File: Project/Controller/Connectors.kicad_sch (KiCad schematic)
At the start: 24 parts, among them J10 Servo, J11 Servo, J12 Servo, J13 Thruster, J14 I2C, J15 I2C, J16 UART1, J17 UART2, J18 SPI1, J19 SPI2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

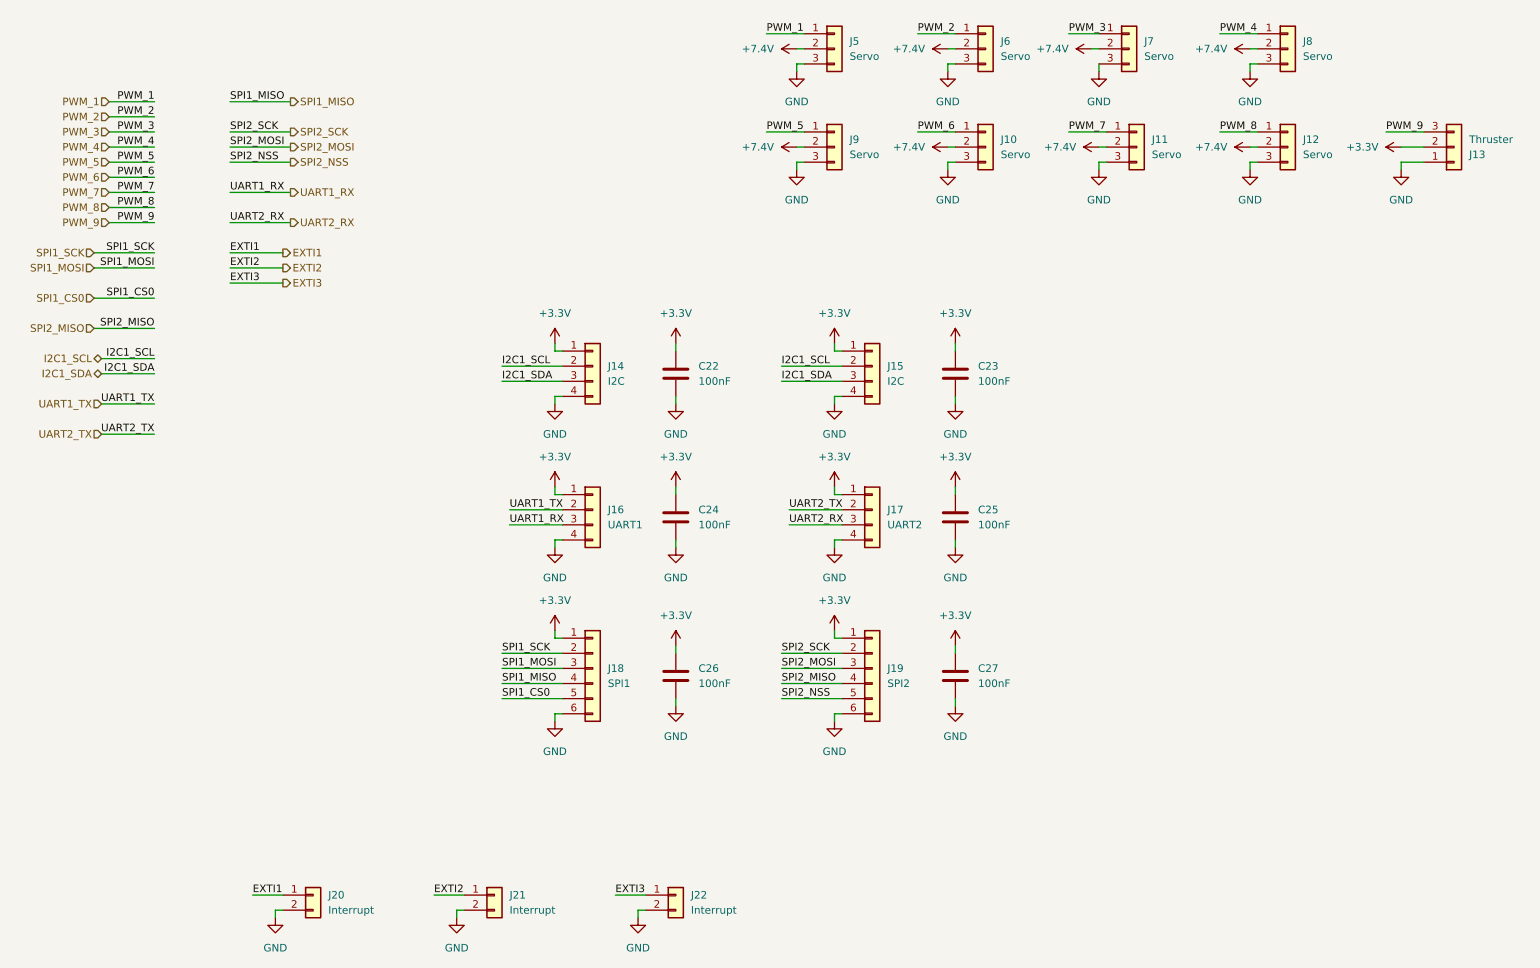
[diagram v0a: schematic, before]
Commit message: Remove battery power from servo PWM connector
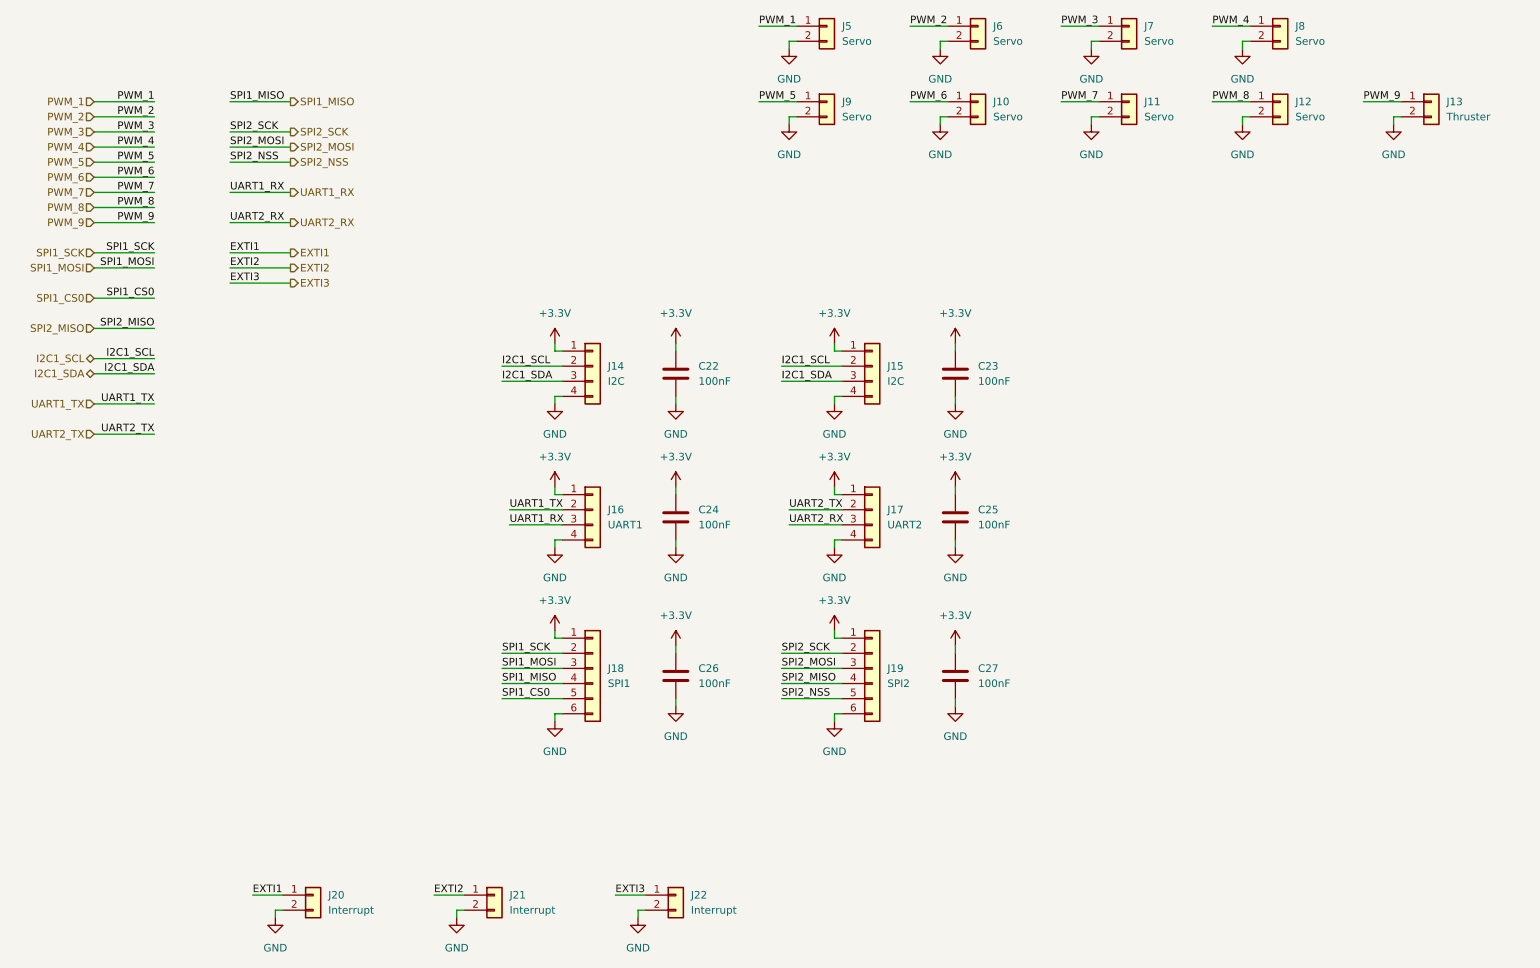
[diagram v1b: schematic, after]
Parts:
- removed J10, J11, J12, J5, J6, J7, J8, J9: Servo, Connector_JST:JST_VH_B3P-VH-B_1x03_P3.96mm_Vertical, symbol Connector_Generic:Conn_01x03
- removed J13: Thruster, Connector_JST:JST_VH_B3P-VH-B_1x03_P3.96mm_Vertical, symbol Connector_Generic:Conn_01x03
- added J10, J11, J12, J5, J6, J7, J8, J9: Servo, Connector_JST:JST_VH_B2P-VH_1x02_P3.96mm_Vertical, symbol Connector_Generic:Conn_01x02
- added J13: Thruster, Connector_JST:JST_VH_B2P-VH_1x02_P3.96mm_Vertical, symbol Connector_Generic:Conn_01x02
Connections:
- net GND: now also J10.2 (Pin_2), J11.2 (Pin_2), J12.2 (Pin_2), J13.2 (Pin_2), J5.2 (Pin_2), J6.2 (Pin_2), J7.2 (Pin_2), J8.2 (Pin_2), J9.2 (Pin_2)
- net PWM_1: now also J5.1 (Pin_1)
- net PWM_2: now also J6.1 (Pin_1)
- net PWM_3: now also J7.1 (Pin_1)
- net PWM_4: now also J8.1 (Pin_1)
- net PWM_5: now also J9.1 (Pin_1)
- net PWM_6: now also J10.1 (Pin_1)
- net PWM_7: now also J11.1 (Pin_1)
- net PWM_8: now also J12.1 (Pin_1)
- net PWM_9: now also J13.1 (Pin_1)

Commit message: Change peripheral connectors to JST GH
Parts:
- J14, J15, J16, J17: footprint Connector_Molex:Molex_PicoBlade_53048-0410_1x04_P1.25mm_Horizontal -> Connector_JST:JST_GH_SM04B-GHS-TB_1x04-1MP_P1.25mm_Horizontal; Listing https://www.digikey.com/en/products/detail/molex/0530480410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 -> https://www.digikey.com/en/products/detail/jst-sales-americ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
- J18, J19: footprint Connector_Molex:Molex_PicoBlade_53048-0610_1x06_P1.25mm_Horizontal -> Connector_JST:JST_GH_SM06B-GHS-TB_1x06-1MP_P1.25mm_Horizontal; Listing https://www.digikey.com/en/products/detail/molex/0530480610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 -> https://www.digikey.com/en/products/detail/jst-sales-americ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
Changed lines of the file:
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@@
 			)
 		)
-		(property "Footprint" "Connector_Molex:Molex_PicoBlade_53048-0610_1x06_P1.25mm_Horizontal"
+		(property "Footprint" "Connector_JST:JST_GH_SM06B-GHS-TB_1x06-1MP_P1.25mm_Horizontal"
 			(at 124.46 133.35 0)
 			(effects
@@
 			)
 		)
-		(property "Datasheet" "https://www.molex.com/content/dam/molex/molex-dot-com/products/automated/en-us/salesdrawingpdf/530/53048/530480610_sd.pdf?inline"
+		(property "Datasheet" "https://www.jst-mfg.com/product/pdf/eng/eGH.pdf"
 			(at 124.46 133.35 0)
 			(effects
@@
 			)
 		)
-		(property "Listing" "https://www.digikey.com/en/products/detail/molex/0530480610/242868"
+		(property "Listing" "https://www.digikey.com/en/products/detail/jst-sales-america-inc/SM06B-GHS-TB/807790"
 			(at 124.46 133.35 0)
 			(effects
@@
 			)
 		)
-		(property "Footprint" "Connector_Molex:Molex_PicoBlade_53048-0410_1x04_P1.25mm_Horizontal"
+		(property "Footprint" "Connector_JST:JST_GH_SM04B-GHS-TB_1x04-1MP_P1.25mm_Horizontal"
 			(at 124.46 106.68 0)
 			(effects
@@
 			)
 		)
-		(property "Datasheet" "https://www.molex.com/content/dam/molex/molex-dot-com/products/automated/en-us/salesdrawingpdf/530/53048/530480410_sd.pdf?inline"
+		(property "Datasheet" "https://www.jst-mfg.com/product/pdf/eng/eGH.pdf"
 			(at 124.46 106.68 0)
 			(effects
@@
 			)
 		)
-		(property "Listing" "https://www.digikey.com/en/products/detail/molex/0530480410/242866"
+		(property "Listing" "https://www.digikey.com/en/products/detail/jst-sales-america-inc/SM04B-GHS-TB/807788"
 			(at 124.46 106.68 0)
 			(effects
@@
 			)
 		)
-		(property "Footprint" "Connector_Molex:Molex_PicoBlade_53048-0410_1x04_P1.25mm_Horizontal"
+		(property "Footprint" "Connector_JST:JST_GH_SM04B-GHS-TB_1x04-1MP_P1.25mm_Horizontal"
 			(at 171.45 82.55 0)
 			(effects
@@
 			)
 		)
-		(property "Datasheet" "https://www.molex.com/content/dam/molex/molex-dot-com/products/automated/en-us/salesdrawingpdf/530/53048/530480410_sd.pdf?inline"
+		(property "Datasheet" "https://www.jst-mfg.com/product/pdf/eng/eGH.pdf"
 			(at 171.45 82.55 0)
 			(effects
@@
 			)
 		)
-		(property "Listing" "https://www.digikey.com/en/products/detail/molex/0530480410/242866"
+		(property "Listing" "https://www.digikey.com/en/products/detail/jst-sales-america-inc/SM04B-GHS-TB/807788"
 			(at 171.45 82.55 0)
 			(effects
@@
 			)
 		)
-		(property "Footprint" "Connector_Molex:Molex_PicoBlade_53048-0410_1x04_P1.25mm_Horizontal"
+		(property "Footprint" "Connector_JST:JST_GH_SM04B-GHS-TB_1x04-1MP_P1.25mm_Horizontal"
 			(at 124.46 82.55 0)
 			(effects
@@
 			)
 		)
-		(property "Datasheet" "https://www.molex.com/content/dam/molex/molex-dot-com/products/automated/en-us/salesdrawingpdf/530/53048/530480410_sd.pdf?inline"
+		(property "Datasheet" "https://www.jst-mfg.com/product/pdf/eng/eGH.pdf"
 			(at 124.46 82.55 0)
 			(effects
@@
 			)
 		)
-		(property "Listing" "https://www.digikey.com/en/products/detail/molex/0530480410/242866"
+		(property "Listing" "https://www.digikey.com/en/products/detail/jst-sales-america-inc/SM04B-GHS-TB/807788"
 			(at 124.46 82.55 0)
 			(effects
@@
 			)
 		)
-		(property "Footprint" "Connector_Molex:Molex_PicoBlade_53048-0610_1x06_P1.25mm_Horizontal"
+		(property "Footprint" "Connector_JST:JST_GH_SM06B-GHS-TB_1x06-1MP_P1.25mm_Horizontal"
 			(at 171.45 133.35 0)
 			(effects
@@
 			)
 		)
-		(property "Datasheet" "https://www.molex.com/content/dam/molex/molex-dot-com/products/automated/en-us/salesdrawingpdf/530/53048/530480610_sd.pdf?inline"
+		(property "Datasheet" "https://www.jst-mfg.com/product/pdf/eng/eGH.pdf"
 			(at 171.45 133.35 0)
 			(effects
@@
 			)
 		)
-		(property "Listing" "https://www.digikey.com/en/products/detail/molex/0530480610/242868"
+		(property "Listing" "https://www.digikey.com/en/products/detail/jst-sales-america-inc/SM06B-GHS-TB/807790"
 			(at 171.45 133.35 0)
 			(effects
@@
 			)
 		)
-		(property "Footprint" "Connector_Molex:Molex_PicoBlade_53048-0410_1x04_P1.25mm_Horizontal"
+		(property "Footprint" "Connector_JST:JST_GH_SM04B-GHS-TB_1x04-1MP_P1.25mm_Horizontal"
 			(at 171.45 106.68 0)
 			(effects
@@
 			)
 		)
-		(property "Datasheet" "https://www.molex.com/content/dam/molex/molex-dot-com/products/automated/en-us/salesdrawingpdf/530/53048/530480410_sd.pdf?inline"
+		(property "Datasheet" "https://www.jst-mfg.com/product/pdf/eng/eGH.pdf"
 			(at 171.45 106.68 0)
 			(effects
@@
 			)
 		)
-		(property "Listing" "https://www.digikey.com/en/products/detail/molex/0530480410/242866"
+		(property "Listing" "https://www.digikey.com/en/products/detail/jst-sales-america-inc/SM04B-GHS-TB/807788"
 			(at 171.45 106.68 0)
 			(effects

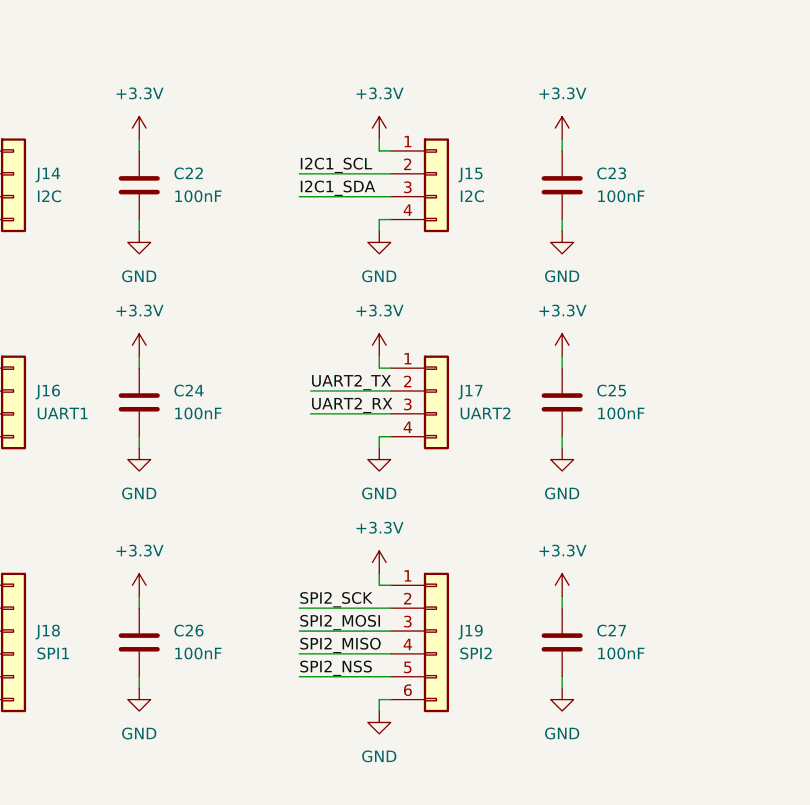
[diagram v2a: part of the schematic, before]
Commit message: Add LDO to power input for controller board
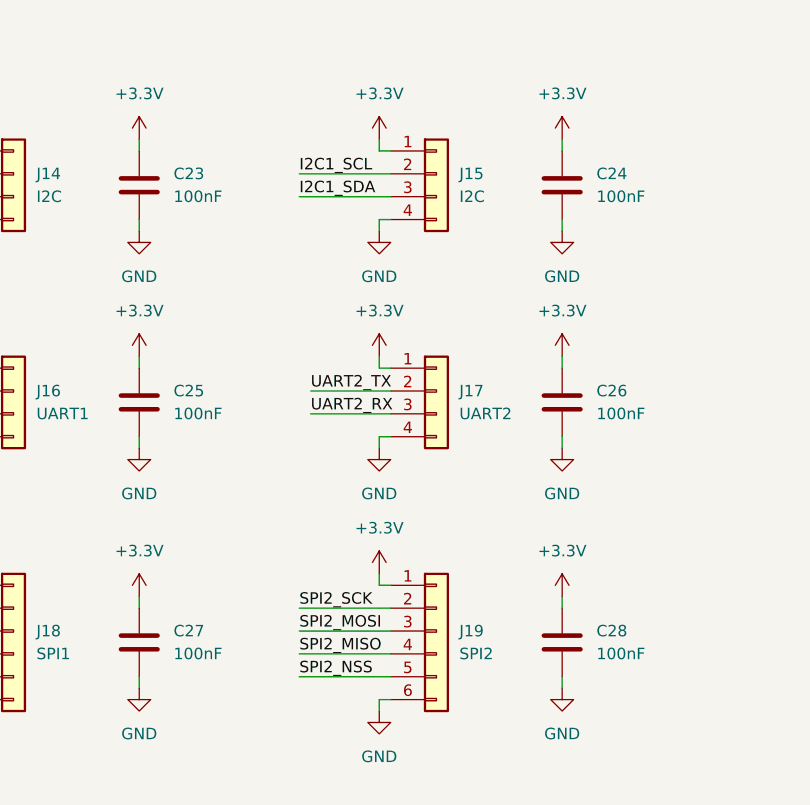
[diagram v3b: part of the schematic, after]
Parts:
- renumbered C22 to C23, C23 to C24, C24 to C25, C25 to C26, C26 to C27, C27 to C28

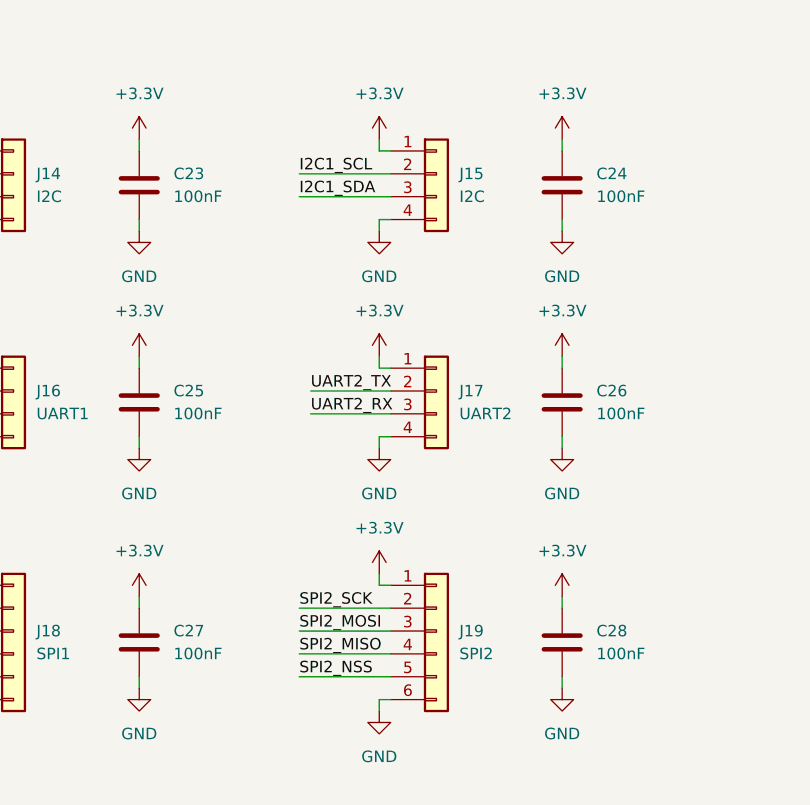
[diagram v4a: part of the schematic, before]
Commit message: Add ideal diode ORing for power connector and USB power
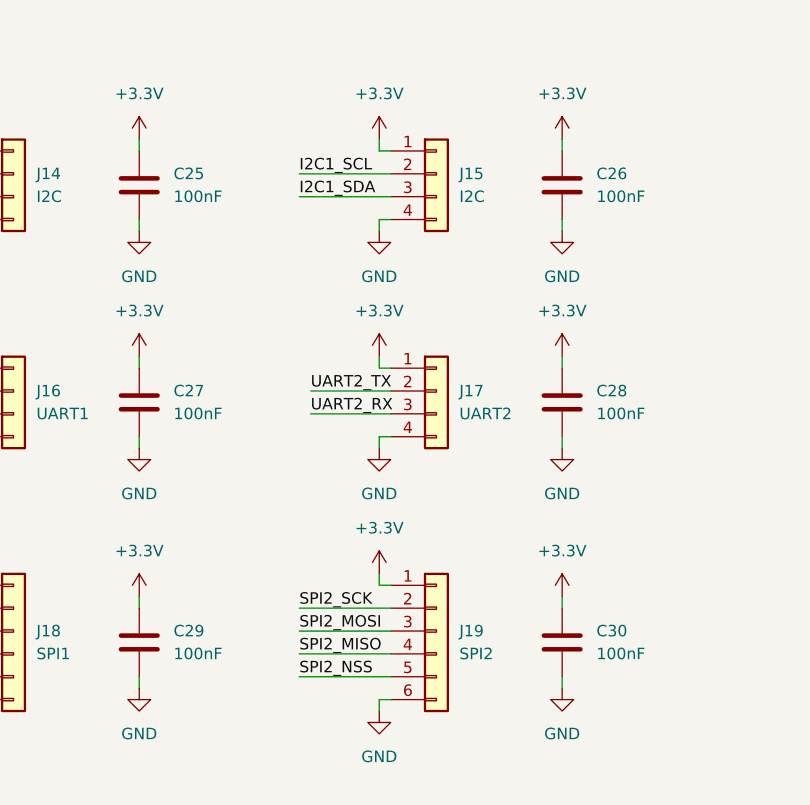
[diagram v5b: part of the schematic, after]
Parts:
- renumbered C23 to C25, C24 to C26, C25 to C27, C26 to C28, C27 to C29, C28 to C30

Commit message: Change 0402 footprints to 0603
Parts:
- C25, C26, C27, C28, C29, C30: footprint Capacitor_SMD:C_0402_1005Metric -> Capacitor_SMD:C_0603_1608Metric; Listing https://www.digikey.com/en/products/detail/samsung-electro-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 -> https://www.digikey.com/en/products/detail/yageo/CC0603KRX7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
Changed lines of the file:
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@@
 			)
 		)
-		(property "Footprint" "Capacitor_SMD:C_0402_1005Metric"
+		(property "Footprint" "Capacitor_SMD:C_0603_1608Metric"
 			(at 139.3952 111.76 0)
 			(effects
@@
 			)
 		)
-		(property "Datasheet" "https://mm.digikey.com/Volume0/opasdata/d220001/medias/docus/503/CL05A104KA5NNNC.pdf"
+		(property "Datasheet" "https://yageogroup.com/download/specsheet/CC0603KRX7R7BB104"
 			(at 138.43 107.95 0)
 			(effects
@@
 			)
 		)
-		(property "Listing" "https://www.digikey.com/en/products/detail/samsung-electro-mechanics/CL05A104KA5NNNC/3886701"
+		(property "Listing" "https://www.digikey.com/en/products/detail/yageo/CC0603KRX7R7BB104/302822"
 			(at 138.43 107.95 0)
 			(effects
@@
 			)
 		)
-		(property "Footprint" "Capacitor_SMD:C_0402_1005Metric"
+		(property "Footprint" "Capacitor_SMD:C_0603_1608Metric"
 			(at 186.3852 87.63 0)
 			(effects
@@
 			)
 		)
-		(property "Datasheet" "https://mm.digikey.com/Volume0/opasdata/d220001/medias/docus/503/CL05A104KA5NNNC.pdf"
+		(property "Datasheet" "https://yageogroup.com/download/specsheet/CC0603KRX7R7BB104"
 			(at 185.42 83.82 0)
 			(effects
@@
 			)
 		)
-		(property "Listing" "https://www.digikey.com/en/products/detail/samsung-electro-mechanics/CL05A104KA5NNNC/3886701"
+		(property "Listing" "https://www.digikey.com/en/products/detail/yageo/CC0603KRX7R7BB104/302822"
 			(at 185.42 83.82 0)
 			(effects
@@
 			)
 		)
-		(property "Footprint" "Capacitor_SMD:C_0402_1005Metric"
+		(property "Footprint" "Capacitor_SMD:C_0603_1608Metric"
 			(at 186.3852 111.76 0)
 			(effects
@@
 			)
 		)
-		(property "Datasheet" "https://mm.digikey.com/Volume0/opasdata/d220001/medias/docus/503/CL05A104KA5NNNC.pdf"
+		(property "Datasheet" "https://yageogroup.com/download/specsheet/CC0603KRX7R7BB104"
 			(at 185.42 107.95 0)
 			(effects
@@
 			)
 		)
-		(property "Listing" "https://www.digikey.com/en/products/detail/samsung-electro-mechanics/CL05A104KA5NNNC/3886701"
+		(property "Listing" "https://www.digikey.com/en/products/detail/yageo/CC0603KRX7R7BB104/302822"
 			(at 185.42 107.95 0)
 			(effects
@@
 			)
 		)
-		(property "Footprint" "Capacitor_SMD:C_0402_1005Metric"
+		(property "Footprint" "Capacitor_SMD:C_0603_1608Metric"
 			(at 139.3952 87.63 0)
 			(effects
@@
 			)
 		)
-		(property "Datasheet" "https://mm.digikey.com/Volume0/opasdata/d220001/medias/docus/503/CL05A104KA5NNNC.pdf"
+		(property "Datasheet" "https://yageogroup.com/download/specsheet/CC0603KRX7R7BB104"
 			(at 138.43 83.82 0)
 			(effects
@@
 			)
 		)
-		(property "Listing" "https://www.digikey.com/en/products/detail/samsung-electro-mechanics/CL05A104KA5NNNC/3886701"
+		(property "Listing" "https://www.digikey.com/en/products/detail/yageo/CC0603KRX7R7BB104/302822"
 			(at 138.43 83.82 0)
 			(effects
@@
 			)
 		)
-		(property "Footprint" "Capacitor_SMD:C_0402_1005Metric"
+		(property "Footprint" "Capacitor_SMD:C_0603_1608Metric"
 			(at 186.3852 138.43 0)
 			(effects
@@
 			)
 		)
-		(property "Datasheet" "https://mm.digikey.com/Volume0/opasdata/d220001/medias/docus/503/CL05A104KA5NNNC.pdf"
+		(property "Datasheet" "https://yageogroup.com/download/specsheet/CC0603KRX7R7BB104"
 			(at 185.42 134.62 0)
 			(effects
@@
 			)
 		)
-		(property "Listing" "https://www.digikey.com/en/products/detail/samsung-electro-mechanics/CL05A104KA5NNNC/3886701"
+		(property "Listing" "https://www.digikey.com/en/products/detail/yageo/CC0603KRX7R7BB104/302822"
 			(at 185.42 134.62 0)
 			(effects
@@
 			)
 		)
-		(property "Footprint" "Capacitor_SMD:C_0402_1005Metric"
+		(property "Footprint" "Capacitor_SMD:C_0603_1608Metric"
 			(at 139.3952 138.43 0)
 			(effects
@@
 			)
 		)
-		(property "Datasheet" "https://mm.digikey.com/Volume0/opasdata/d220001/medias/docus/503/CL05A104KA5NNNC.pdf"
+		(property "Datasheet" "https://yageogroup.com/download/specsheet/CC0603KRX7R7BB104"
 			(at 138.43 134.62 0)
 			(effects
@@
 			)
 		)
-		(property "Listing" "https://www.digikey.com/en/products/detail/samsung-electro-mechanics/CL05A104KA5NNNC/3886701"
+		(property "Listing" "https://www.digikey.com/en/products/detail/yageo/CC0603KRX7R7BB104/302822"
 			(at 138.43 134.62 0)
 			(effects
